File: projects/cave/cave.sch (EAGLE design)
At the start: 122 parts, among them U1 IRLML6344TRPBF, U10 IRLML6344TRPBF, U11 IRLML6344TRPBF, U12 IRLML6344TRPBF, U2 TLC555CDR, U3 IRLML6344TRPBF, U4 IRLML6344TRPBF, U5 IRLML6344TRPBF, U6 IRLML6344TRPBF, U7 TPS54625, U8 IRLML6344TRPBF, U9 IRLML6344TRPBF

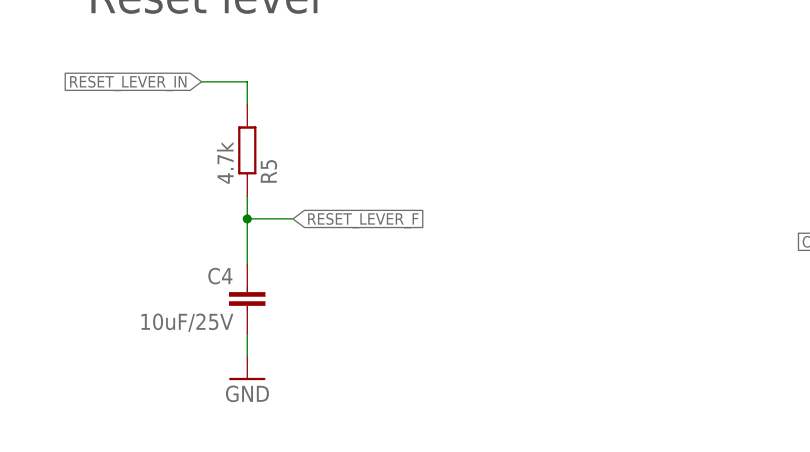
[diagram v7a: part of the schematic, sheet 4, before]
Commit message: GPIO for reset_lever is pulled up on the RPi, so we need to pull it down...
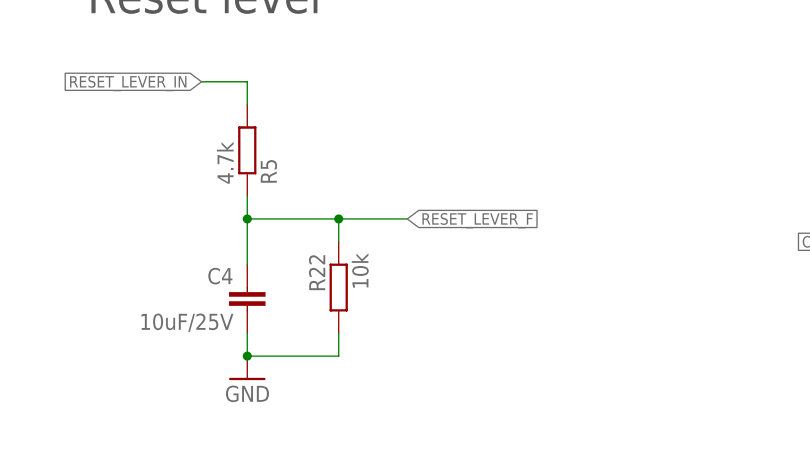
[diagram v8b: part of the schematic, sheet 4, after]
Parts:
- added R22: 10k, rcl:R-EU_R0603
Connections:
- net GND: now also R22.2
- net RESET_LEVER_F: now also R22.1
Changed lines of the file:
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@@
 <part name="R14" library="rcl" deviceset="R-EU_" device="R0603" value="100k"/>
 <part name="C17" library="rcl" deviceset="C-EU" device="C0603" value="0.1uF/25V"/>
+<part name="R22" library="rcl" deviceset="R-EU_" device="R0603" value="10k"/>
 </parts>
 <sheets>
@@
 <instance part="R14" gate="G$1" x="177.8" y="127" rot="MR180"/>
 <instance part="C17" gate="G$1" x="190.5" y="121.92" rot="MR0"/>
+<instance part="R22" gate="G$1" x="15.24" y="35.56" rot="MR270"/>
 </instances>
 <busses>
@@
 <wire x1="5.08" y1="27.94" x2="5.08" y2="30.48" width="0.1524" layer="91"/>
 <pinref part="GND6" gate="1" pin="GND"/>
+<pinref part="R22" gate="G$1" pin="2"/>
+<wire x1="15.24" y1="30.48" x2="15.24" y2="27.94" width="0.1524" layer="91"/>
+<wire x1="15.24" y1="27.94" x2="5.08" y2="27.94" width="0.1524" layer="91"/>
+<junction x="5.08" y="27.94"/>
 </segment>
 <segment>
@@
 <wire x1="5.08" y1="45.72" x2="5.08" y2="43.18" width="0.1524" layer="91"/>
 <wire x1="5.08" y1="43.18" x2="5.08" y2="38.1" width="0.1524" layer="91"/>
-<wire x1="5.08" y1="43.18" x2="10.16" y2="43.18" width="0.1524" layer="91"/>
+<wire x1="5.08" y1="43.18" x2="15.24" y2="43.18" width="0.1524" layer="91"/>
 <junction x="5.08" y="43.18"/>
-<label x="10.16" y="43.18" size="1.27" layer="95" xref="yes"/>
-</segment>
-</net>
+<label x="22.86" y="43.18" size="1.27" layer="95" xref="yes"/>
+<pinref part="R22" gate="G$1" pin="1"/>
+<wire x1="15.24" y1="43.18" x2="22.86" y2="43.18" width="0.1524" layer="91"/>
+<wire x1="15.24" y1="40.64" x2="15.24" y2="43.18" width="0.1524" layer="91"/>
+<junction x="15.24" y="43.18"/>
+</segment>
+</net>
